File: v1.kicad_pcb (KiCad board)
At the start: 4 copper layers, 200 x 150 mm, 416 parts, among them J10 Conn_Coaxial, J11 USB_B_Micro, J12 Micro_SD_Card_Det, J13 ARJM11D7-502-AB-EW2, J14 USB_A, J15 HDMI_A, J16 Conn_Coaxial, J2 Barrel_Jack_Switch, J3 Conn_01x02, J4 Conn_01x02, J5 Conn_01x02, J6 Conn_01x02, J7 Conn_01x02, J8 Conn_01x06_Male, J9 Conn_Coaxial, M1 Logo_16mmx16mm, Q1 Si7141DP, Q10 Si7141DP, Q11 SI1539CDL-T1-GE3, Q12 SI1539CDL-T1-GE3, Q13 SI1539CDL-T1-GE3, Q2 SI1539CDL-T1-GE3, Q3 Si7141DP, Q4 SI1539CDL-T1-GE3, Q5 Si7141DP, Q6 Si7141DP, Q7 SI1539CDL-T1-GE3, Q8 Si7141DP, Q9 SI1539CDL-T1-GE3, SW1 SW_SPDT, SW2 Tactile_Switch_Generic, T1 PWB2010L, T2 Macom_ETC1-1-13, T3 PWB2010L, U1 171050601, U10 MAX9612, U11 ADM7154, U12 MAX9612, U13 TPS3701DDCR, U14 LCMXO2-640HC-4SG48C, U15 REF5025IDGK, U16 LTC2216, U17 TE0720, U18 JTAG-SMT3, U19 TPD2S017, U2 MAX9612, U20 TXS02612, U21 TPS2051B, U22 TPD2S017, U23 TFP410PAP, U24 TLC59281RGER, U25 TLC59281RGER, U26 TLC59281RGER, U27 TLC59281RGER, U28 TLC59281RGER, U3 TPS3701DDCR, U30 AD9744_LFCSP, U31 ADR280RT, U4 171050601, U5 MAX9612, U6 TPS3701DDCR, U7 NCP1117-3.3_TO252, U8 MAX9612, U9 TPS3701DDCR, Y1 SIT5001AC-3E-33N0-80.000000X

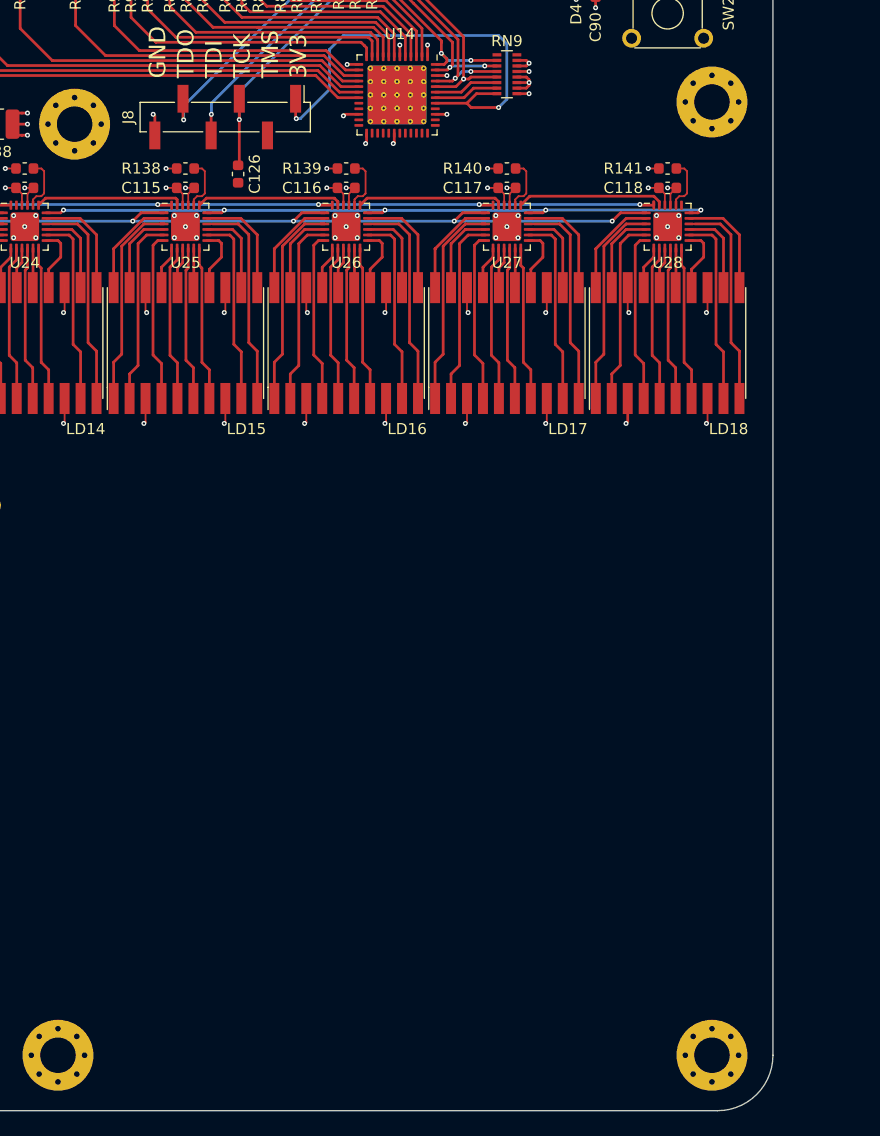
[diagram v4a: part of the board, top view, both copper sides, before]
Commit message: started adding AF ADC/DAC
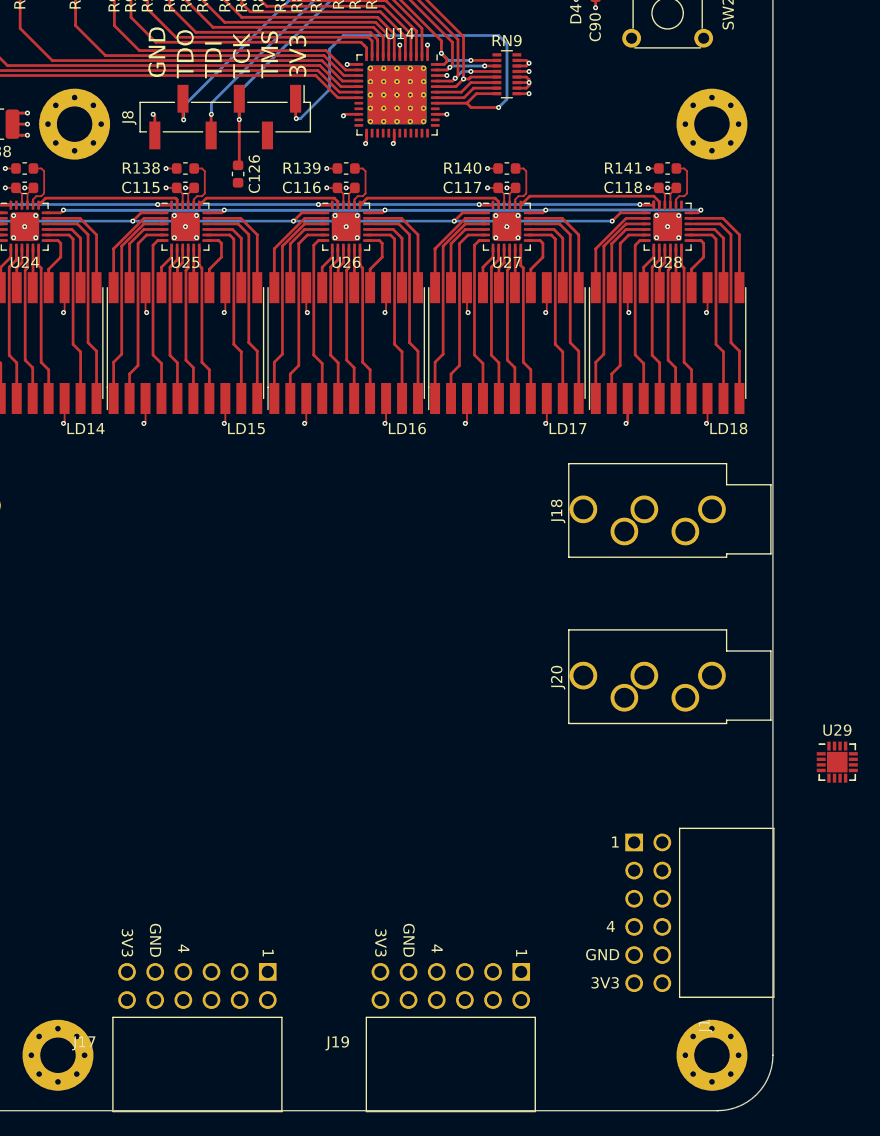
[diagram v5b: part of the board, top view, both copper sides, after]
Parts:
- added J1: Connector_PMOD_2x6_Host, Connector_WUT:PMOD_Wurth_613012243121_Horizontal_Host, F.Cu at (236.2, 158.2)
- added J17: Connector_PMOD_2x6_Host, Connector_WUT:PMOD_Wurth_613012243121_Horizontal_Host, F.Cu at (195.6, 164.8)
- added J18: SJ1-3535NG-BE, Connector_WUT:Jack_3.5mm_CUI_SJ1-3535NG-BE_Horizontal_CircularHoles_Blue, F.Cu at (242.0, 121.8)
- added J19: Connector_PMOD_2x6_Host, Connector_WUT:PMOD_Wurth_613012243121_Horizontal_Host, F.Cu at (218.4, 164.8)
- added J20: SJ1-3535NG-GR, Connector_WUT:Jack_3.5mm_CUI_SJ1-3535NG-GR_Horizontal_CircularHoles_Green, F.Cu at (242.0, 136.8)
- added U29: AD5689BCPZ, Package_CSP:LFCSP-16-1EP_3x3mm_P0.5mm_EP1.854x1.854mm, F.Cu at (253.3, 144.6)
- moved H5 2.00 mm to (242.0, 87.0)
